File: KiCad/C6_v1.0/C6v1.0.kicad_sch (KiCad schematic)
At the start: 4 parts

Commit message: plz
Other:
- added sheet power (untitled.kicad_sch)
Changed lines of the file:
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@@
+	)
+	(sheet
+		(at 190.5 43.18)
+		(size 44.45 29.21)
+		(exclude_from_sim no)
+		(in_bom yes)
+		(on_board yes)
+		(dnp no)
+		(fields_autoplaced yes)
+		(stroke
+			(width 0.1524)
+			(type solid)
+		)
+		(fill
+			(color 0 0 0 0.0000)
+		)
+		(property "Sheetname" "power"
+			(at 190.5 42.4684 0)
+			(effects
+				(font
+					(size 1.27 1.27)
+				)
+				(justify left bottom)
+			)
+		)
+		(property "Sheetfile" "untitled.kicad_sch"
+			(at 190.5 72.9746 0)
+			(effects
+				(font
+					(size 1.27 1.27)
+				)
+				(justify left top)
+			)
+		)
+		(instances
+			(project "C6v1.0"
+				(path "/8737aa07-2805-4383-a805-a4fb57529a3e"
+					(page "8")
+				)
+			)
+		)
 	)
 	(sheet

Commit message: commit gng gng
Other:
- sheet power renamed Power
- sheet Power: file untitled.kicad_sch -> Power.kicad_sch
- sheet Power ports: added 1V8, 2V8, 3V3, 5V, 8V4, GND, RRC3_RX, RRC3_TX; removed none

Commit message: pingus
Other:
- sheet Power ports: added none; removed RRC3_RX, RRC3_TX
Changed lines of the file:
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@@
+	(wire
+		(pts
+			(xy 177.8 101.6) (xy 182.88 101.6)
+		)
+		(stroke
+			(width 0)
+			(type default)
+		)
+	)
 	(wire
 		(pts
@@
 	(wire
 		(pts
+			(xy 182.88 101.6) (xy 182.88 104.14)
+		)
+		(stroke
+			(width 0)
+			(type default)
+		)
+	)
+	(wire
+		(pts
 			(xy 20.32 83.82) (xy 25.4 83.82)
 		)
@@
 	(wire
 		(pts
-			(xy 187.96 69.85) (xy 190.5 69.85)
-		)
-		(stroke
-			(width 0)
-			(type default)
-		)
-	)
-	(wire
-		(pts
 			(xy 139.7 78.74) (xy 144.78 78.74)
 		)
@@
 		(pts
 			(xy 20.32 129.54) (xy 25.4 129.54)
-		)
-		(stroke
-			(width 0)
-			(type default)
-		)
-	)
-	(wire
-		(pts
-			(xy 187.96 67.31) (xy 190.5 67.31)
 		)
 		(stroke
@@
 		)
 	)
-	(label "RRC3_TX"
-		(at 187.96 69.85 180)
-		(effects
-			(font
-				(size 1.27 1.27)
-			)
-			(justify right bottom)
-		)
-	)
 	(label "CAM_SDA"
 		(at 20.32 83.82 180)
@@
 		)
 	)
-	(label "RRC3_RX"
-		(at 187.96 67.31 180)
-		(effects
-			(font
-				(size 1.27 1.27)
-			)
-			(justify right bottom)
-		)
-	)
 	(label "3V3"
 		(at 20.32 50.8 180)
@@
 			)
 			(justify left bottom)
+		)
+	)
+	(label "GND"
+		(at 177.8 101.6 180)
+		(effects
+			(font
+				(size 1.27 1.27)
+			)
+			(justify right bottom)
 		)
 	)
@@
 	)
 	(symbol
+		(lib_id "power:GND")
+		(at 182.88 104.14 0)
+		(unit 1)
+		(exclude_from_sim no)
+		(in_bom yes)
+		(on_board yes)
+		(dnp no)
+		(fields_autoplaced yes)
+		(property "Reference" "#PWR020"
+			(at 182.88 110.49 0)
+			(effects
+				(font
+					(size 1.27 1.27)
+				)
+				(hide yes)
+			)
+		)
+		(property "Value" "GND"
+			(at 182.88 109.22 0)
+			(effects
+				(font
+					(size 1.27 1.27)
+				)
+			)
+		)
+		(property "Footprint" ""
+			(at 182.88 104.14 0)
+			(effects
+				(font
+					(size 1.27 1.27)
+				)
+				(hide yes)
+			)
+		)
+		(property "Datasheet" ""
+			(at 182.88 104.14 0)
+			(effects
+				(font
+					(size 1.27 1.27)
+				)
+				(hide yes)
+			)
+		)
+		(property "Description" "Power symbol creates a global label with name \"GND\" , ground"
+			(at 182.88 104.14 0)
+			(effects
+				(font
+					(size 1.27 1.27)
+				)
+				(hide yes)
+			)
+		)
+		(pin "1"
+		)
+		(instances
+			(project ""
+				(path "/8737aa07-2805-4383-a805-a4fb57529a3e"
+					(reference "#PWR020")
+					(unit 1)
+				)
+			)
+		)
+	)
+	(symbol
 		(lib_id "Mechanical:MountingHole")
 		(at 25.4 152.4 0)
@@
 			(effects
 				(font
-					(size 1.27 1.27)
-				)
-				(justify left)
-			)
-		)
-		(pin "RRC3_RX" output
-			(at 190.5 67.31 180)
-			(effects
-				(font
-					(size 1.27 1.27)
-				)
-				(justify left)
-			)
-		)
-		(pin "RRC3_TX" input
-			(at 190.5 69.85 180)
-			(effects
-				(font

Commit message: yay
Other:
- sheet Power ports: added ADC, EGSE_RX, EGSE_TX, I2C_SCL, I2C_SDA; removed none
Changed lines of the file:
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@@
+			)
+		)
+		(pin "ADC" input
+			(at 190.5 53.34 180)
+			(effects
+				(font
+					(size 1.27 1.27)
+				)
+				(justify left)
+			)
+		)
+		(pin "EGSE_RX" input
+			(at 190.5 57.15 180)
+			(effects
+				(font
+					(size 1.27 1.27)
+				)
+				(justify left)
+			)
+		)
+		(pin "EGSE_TX" input
+			(at 190.5 59.69 180)
+			(effects
+				(font
+					(size 1.27 1.27)
+				)
+				(justify left)
+			)
+		)
+		(pin "I2C_SCL" input
+			(at 190.5 63.5 180)
+			(effects
+				(font
+					(size 1.27 1.27)
+				)
+				(justify left)
+			)
+		)
+		(pin "I2C_SDA" input
+			(at 190.5 66.04 180)
+			(effects
+				(font
+					(size 1.27 1.27)
+				)
+				(justify left)
 			)
 		)

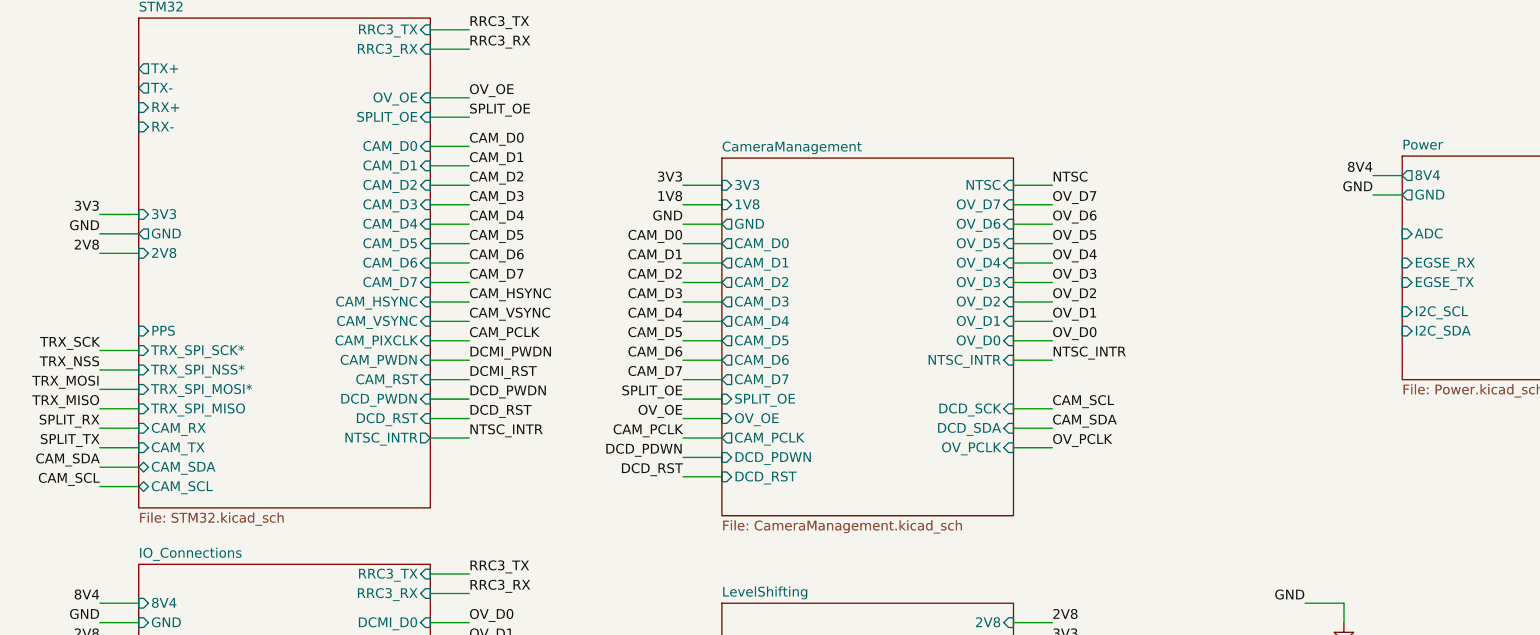
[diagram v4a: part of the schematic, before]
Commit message: made voltage sense more accurate to 1%
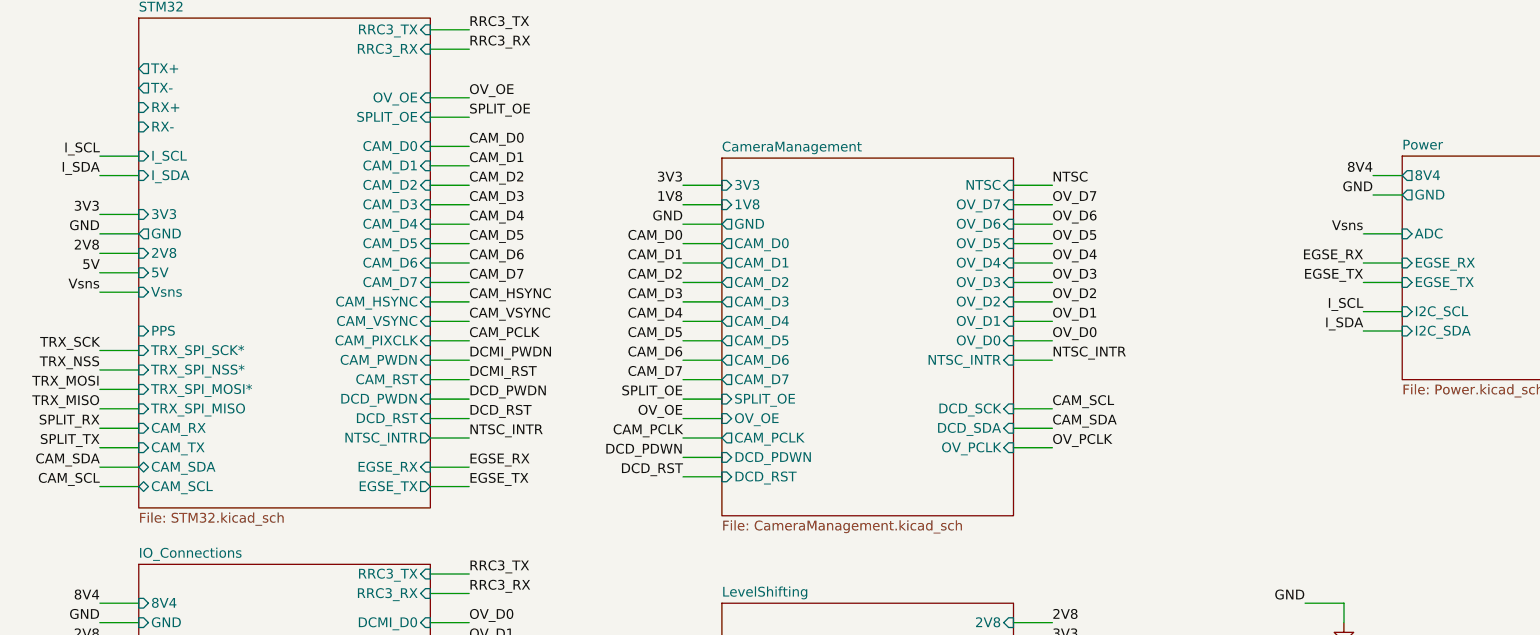
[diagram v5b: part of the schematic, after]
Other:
- sheet STM32 ports: added 5V, EGSE_RX, EGSE_TX, I_SCL, I_SDA, Vsns; removed none

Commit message: DCMI1-Me0
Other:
- sheet IO_Connections ports: added 3V3, ESC_TLM, HALL_A, HALL_B, HALL_C, PPS, PWM_IN, RX+, RX-, TX+, TX-; removed none
- sheet STM32 ports: added ESC_PWM, ESC_TLM, HALL_A, HALL_B, HALL_C; removed none
- moved on the sheet: H1, H2, H3, H4

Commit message: finaly
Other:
- sheet CameraManagement ports: added CAM_D0*, CAM_D1*, CAM_D2*, CAM_D3*, CAM_D4*, CAM_D5*, CAM_D6*, CAM_D7*, CAM_HSYNC*, CAM_PCLK*, CAM_PDWN*, CAM_S, CAM_VSYNC*, OV_HSYNC, OV_PWDN, OV_VSYNC; removed CAM_D0, CAM_D1, CAM_D2, CAM_D3, CAM_D4, CAM_D5, CAM_D6, CAM_D7, CAM_PCLK, DCD_PDWN, OV_OE, SPLIT_OE
- sheet STM32 ports: added none; removed DCD_PWDN, SPLIT_OE
